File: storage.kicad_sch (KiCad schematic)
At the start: 14 parts, among them J11 microSD, Molex 104031-0811 pu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, U24 DNP: W25Q64JVSSIQ, 64 Mbit QS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

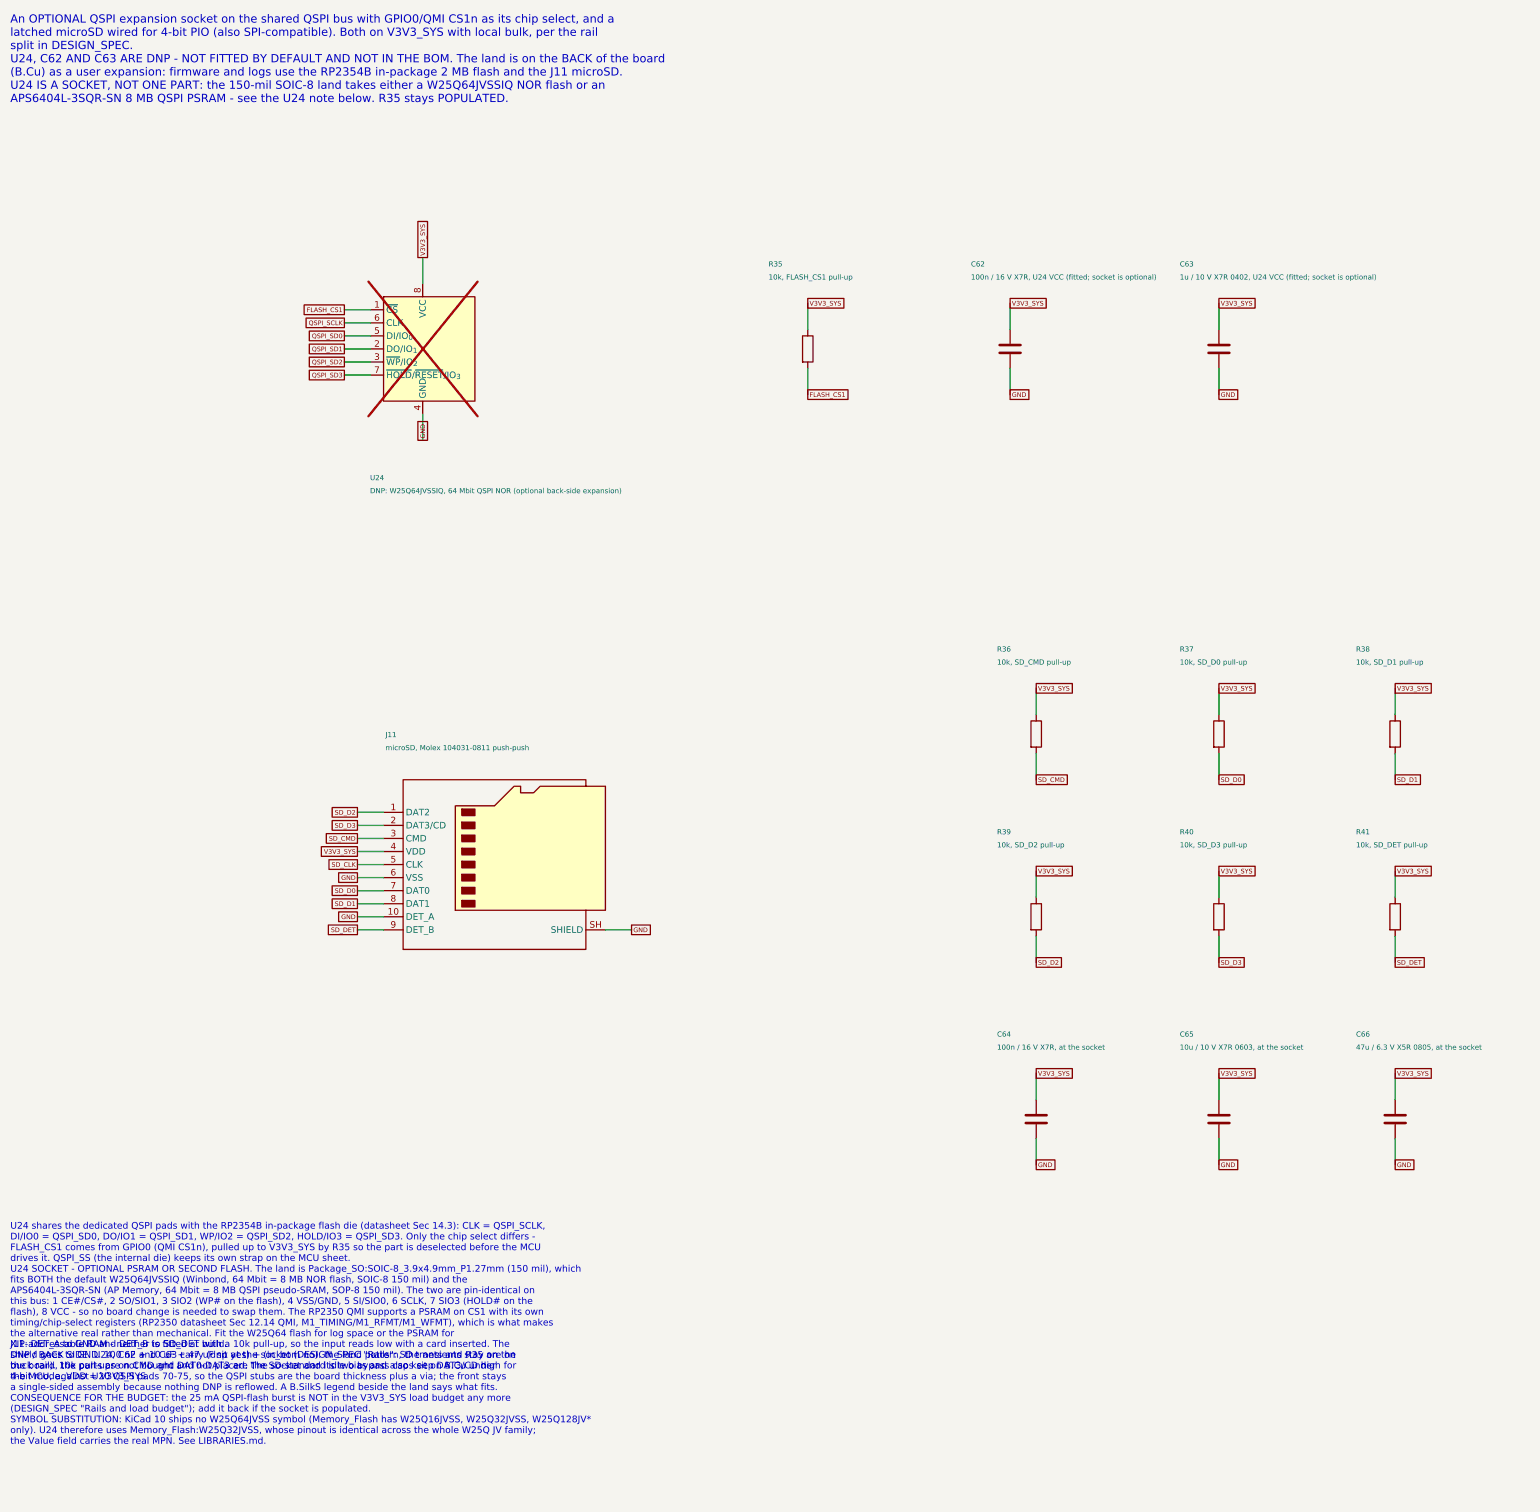
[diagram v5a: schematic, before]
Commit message: JLCPCB sourcing: Basic-part refactor, LCSC numbers in the schematic, order files and audit
Parts audited line by line against JLCPCB's live catalogue (tools/jlc/,
reports/jlc-audit.md). Resistors move 0201 -> 0402 (JLC's Basic library has
no 0201 resistor), the U7 FB divider becomes 10k/3.16k 0.1 % (15.8k 0.1 % is
not stocked), Y1 becomes TAXM12M4RFBCCT2T (CL 12 pF) with 18 pF loads, L2/L3
become CJIANG FTC303020D2R2MBCA / FTC404030S4R7MGCA (stocked; Isat 5.5 A /
6.0 A at 30 %, footprints + models vendored from KiCad), the 22 uF/25 V and
10 uF lines move to Basic parts. The U24 default fit is W25Q32JVSNIQ (the
W25Q64JVSSIQ is a 208-mil part and never fitted the 150-mil socket).

Every fitted symbol carries a hidden LCSC property stamped from
tools/jlc/lcsc_map.csv; tools/jlc/export_jlc.py writes reports/jlc-bom.csv
and reports/jlc-cpl.csv (top-side SMT, headers unpopulated, U24 DNP).
Result: 46 unique parts, 16 Basic / 1 Preferred / 29 Extended (was 9/1/35),
extended-fee estimate $87 (was $105), $45.68 per board at 10 (was $52.97 with
L2 unsourced). DESIGN_SPEC gains a Manufacturing (JLCPCB) section with the
quote parameters. Board rebuilt (0 fit/geometry, DRC unrouted-only); ERC
0/0, checker PASS, ngspice PASS, audit 140/140.

Co-Authored-By: Claude Fable 5.1 <noreply@anthropic.com>
Claude-Session: https://claude.ai/code/session_01U6Ud7JA3CDTJZVcZZr5sx1
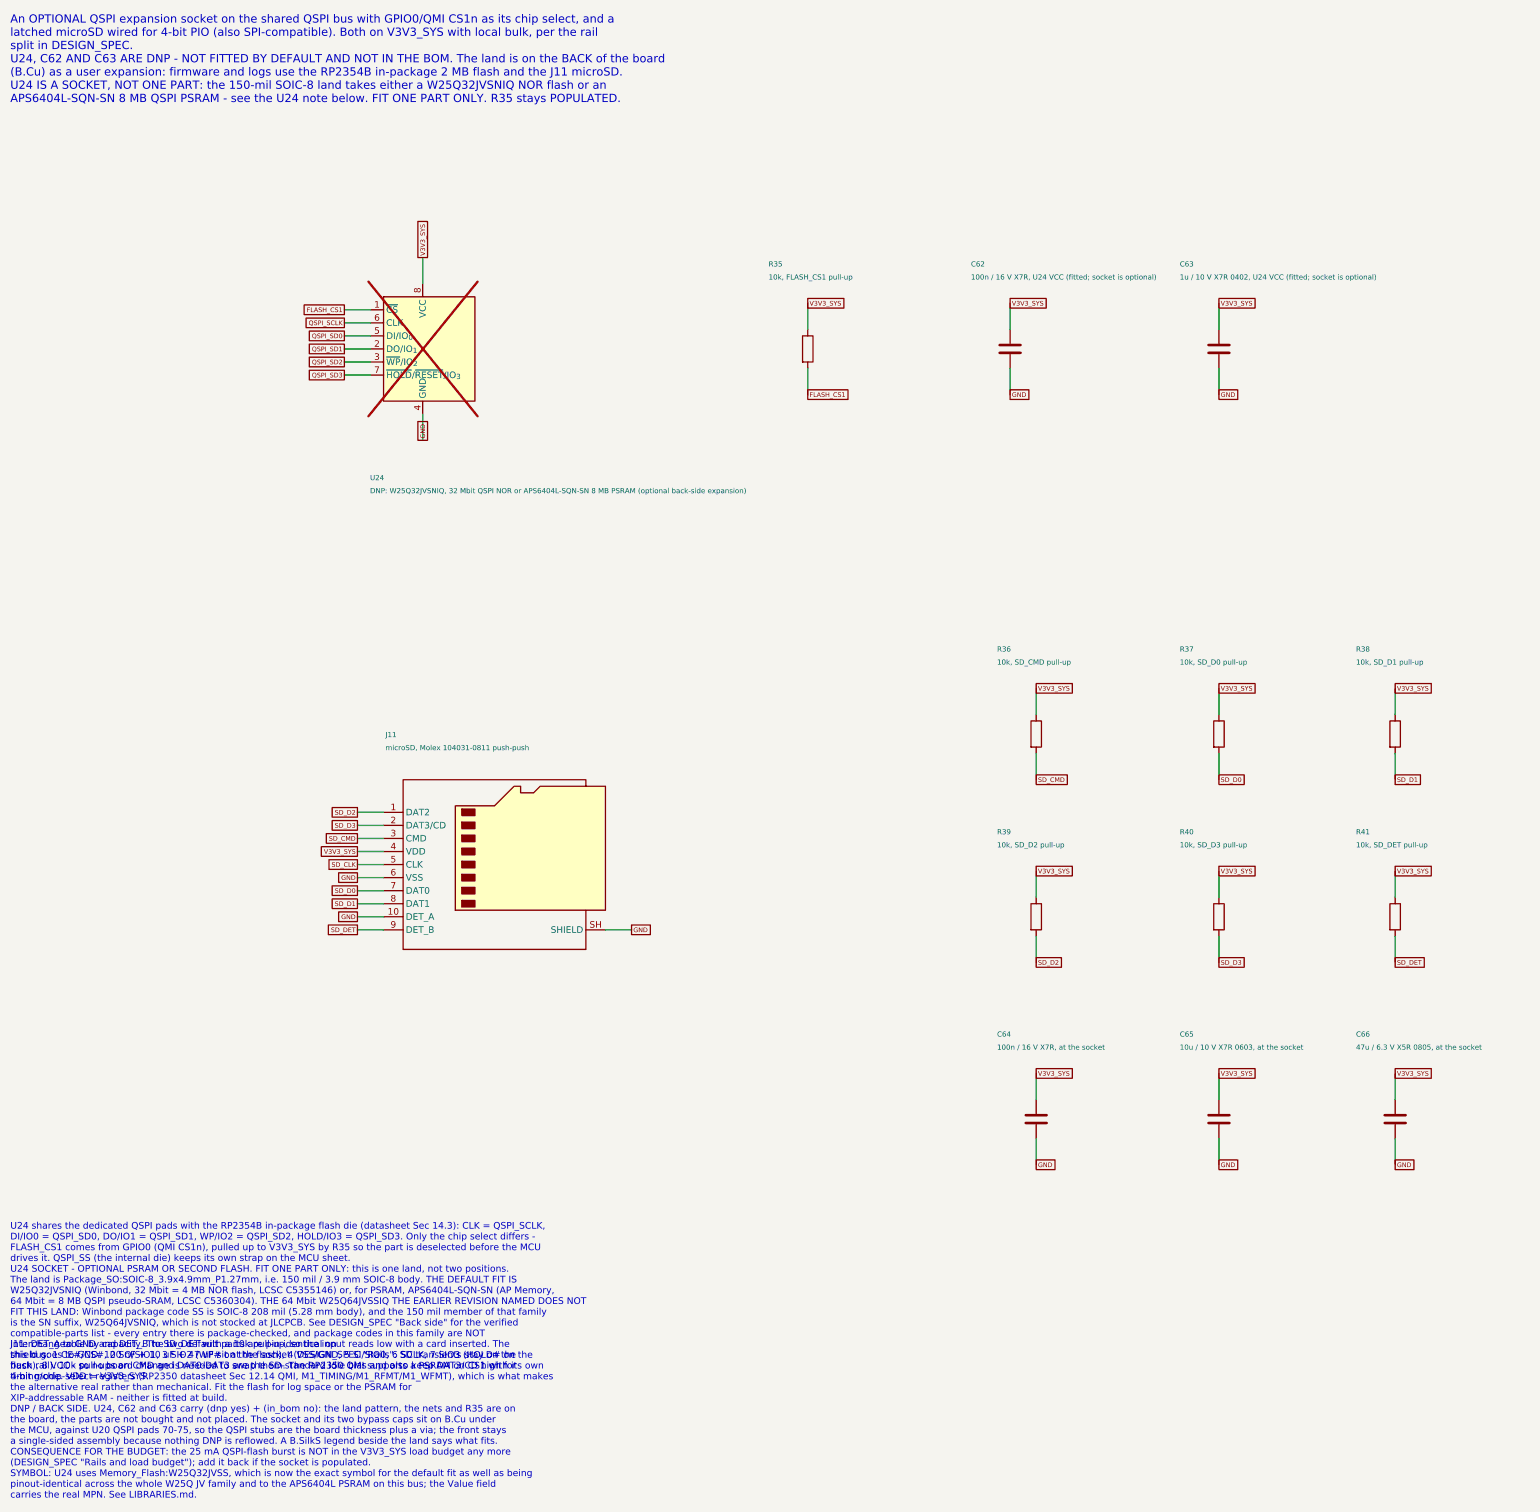
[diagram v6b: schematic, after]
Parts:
- C62, C64: LCSC (none) -> C1525
- C63: LCSC (none) -> C52923
- C65: LCSC (none) -> C96446
- C66: LCSC (none) -> C16780
- J11: LCSC (none) -> C585350
- R35, R36, R37, R38, R39, R40, R41: footprint Resistor_SMD:R_0201_0603Metric -> Resistor_SMD:R_0402_1005Metric; LCSC (none) -> C25744
- U24: value DNP: W25Q64JVSSIQ, 64 Mbit QSPI NOR (optional back-side expansion) -> DNP: W25Q32JVSNIQ, 32 Mbit QSPI NOR or APS6404L-SQN-SN 8 MB PSRAM (optional back-side expansion)
